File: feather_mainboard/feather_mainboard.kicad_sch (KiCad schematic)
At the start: 0 parts

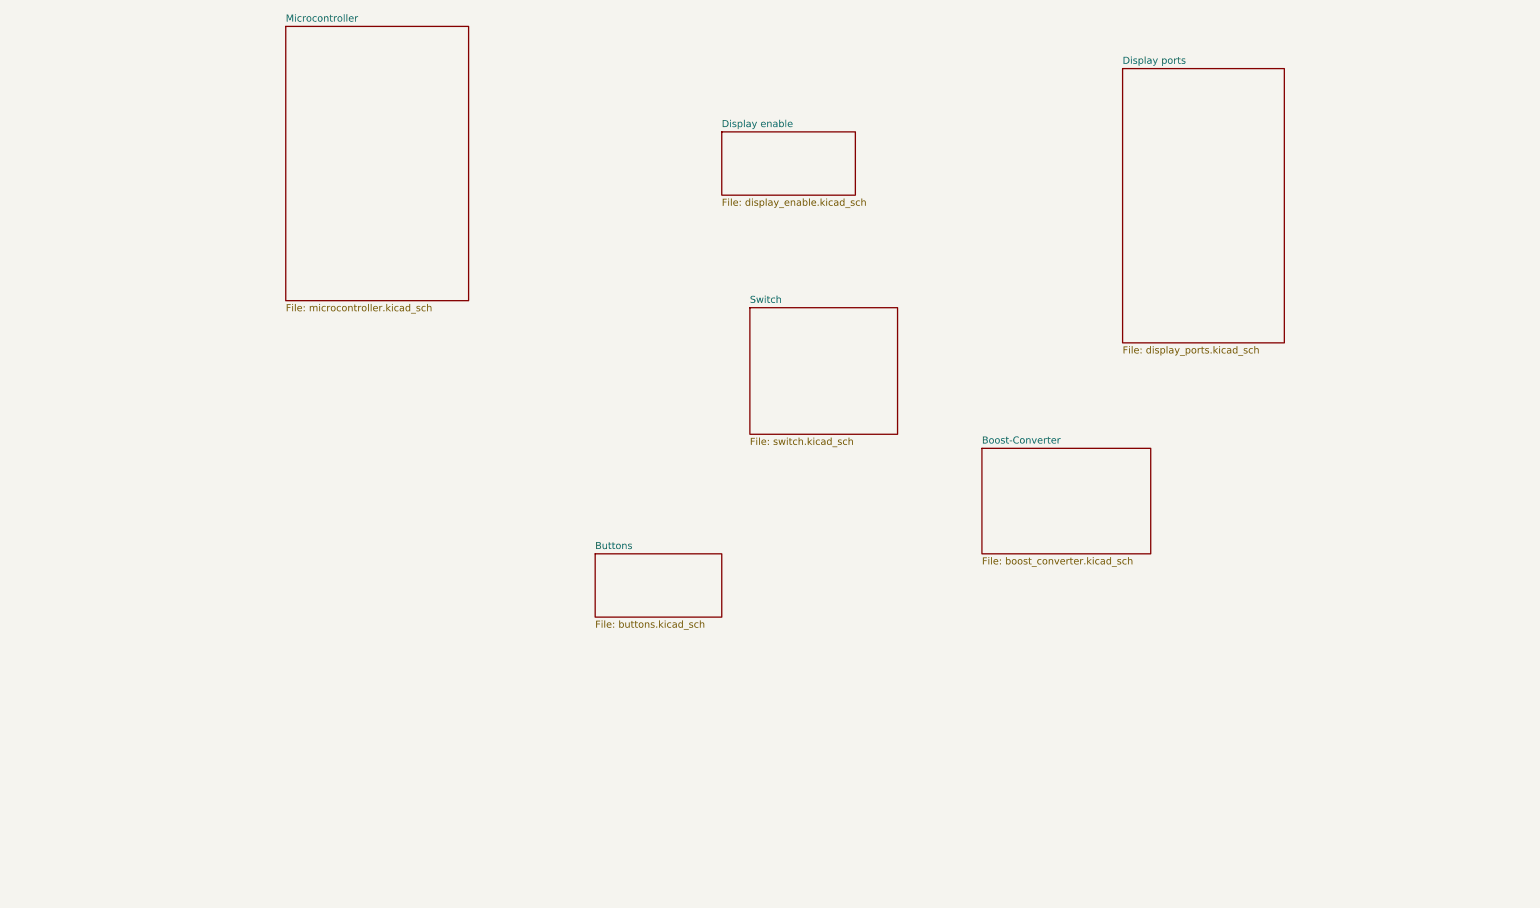
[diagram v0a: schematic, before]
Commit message: finished microcontroller and microsd card subsheets. TODO: button subsheets and internal connections
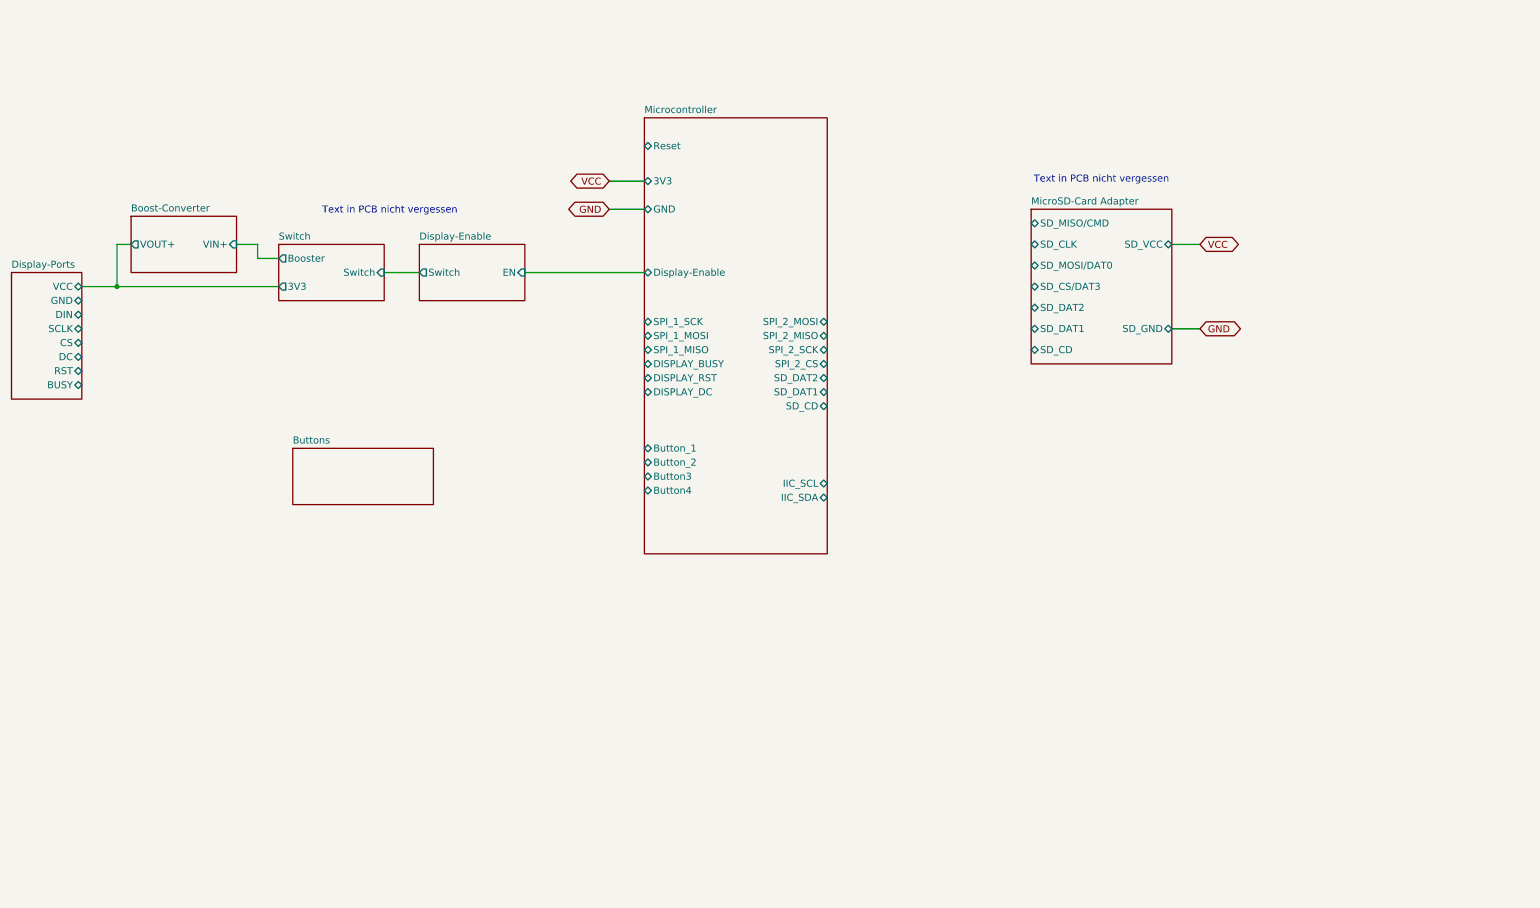
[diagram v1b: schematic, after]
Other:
- sheet Display enable renamed Display-Enable
- sheet Display ports renamed Display-Ports
- added sheet MicroSD-Card Adapter (microsd-card_adapter.kicad_sch)
- sheet Boost-Converter ports: added VIN+, VOUT+; removed none
- sheet Display-Enable ports: added EN, Switch; removed none
- sheet Display-Ports ports: added BUSY, CS, DC, DIN, GND, RST, SCLK, VCC; removed none
- sheet Microcontroller ports: added 3V3, Button3, Button4, Button_1, Button_2, DISPLAY_BUSY, DISPLAY_DC, DISPLAY_RST, Display-Enable, GND, IIC_SCL, IIC_SDA, Reset, SD_CD, SD_DAT1, SD_DAT2, SPI_1_MISO, SPI_1_MOSI, SPI_1_SCK, SPI_2_CS, SPI_2_MISO, SPI_2_MOSI, SPI_2_SCK; removed none
- sheet Switch ports: added 3V3, Booster, Switch; removed none
- note added: "Text in PCB nicht vergessen"

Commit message: schematic is almost done (check TODOs in schematic file)
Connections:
- no-connect marks 0 -> 3
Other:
- added sheet Reset-Button (reset-button.kicad_sch)
- sheet Buttons ports: added Button_1, Button_2, Button_3; removed none
- sheet Microcontroller ports: added Button_3, DISPLAY_CS, DISPLAY_MOSI, DISPLAY_SCLK, Free, SD_CLK, SD_CS/DAT3, SD_MISO/CMD, SD_MOSI/DAT0; removed Button3, Button4, SPI_1_MISO, SPI_1_MOSI, SPI_1_SCK, SPI_2_CS, SPI_2_MISO, SPI_2_MOSI, SPI_2_SCK
- note added: "TODOs: Schematic: - Change the buttons to the correct ones!!! - Pogo-Pin Magnets PCB Design: - Mounting Holes - Messpunkte - Text in PCB für Switches schreiben"
- note removed: "Text in PCB nicht vergessen"

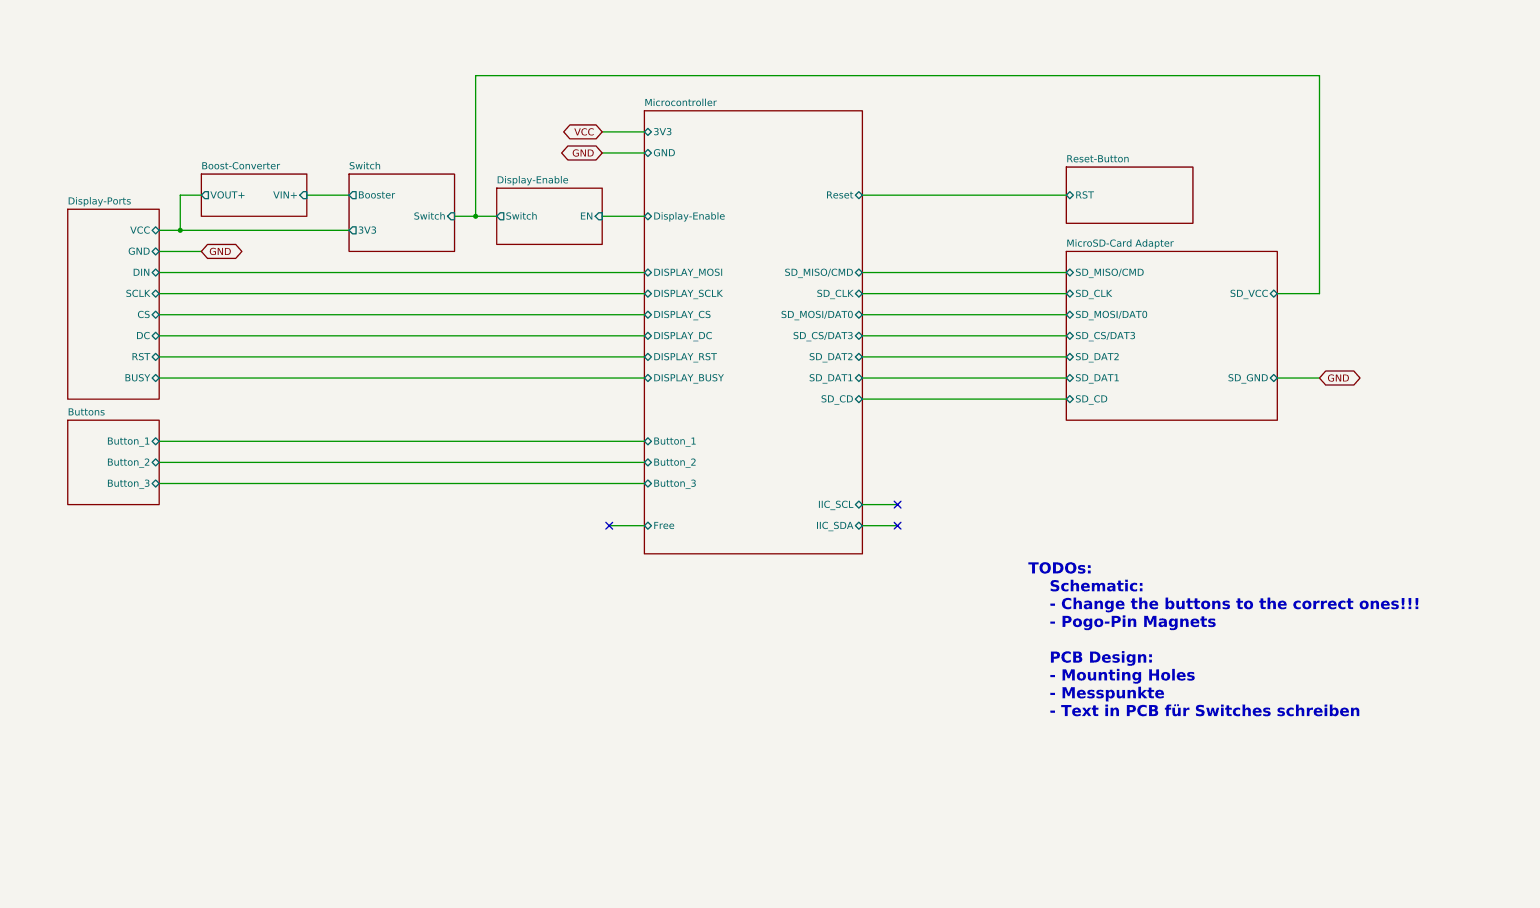
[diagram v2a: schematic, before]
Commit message: added daughter board
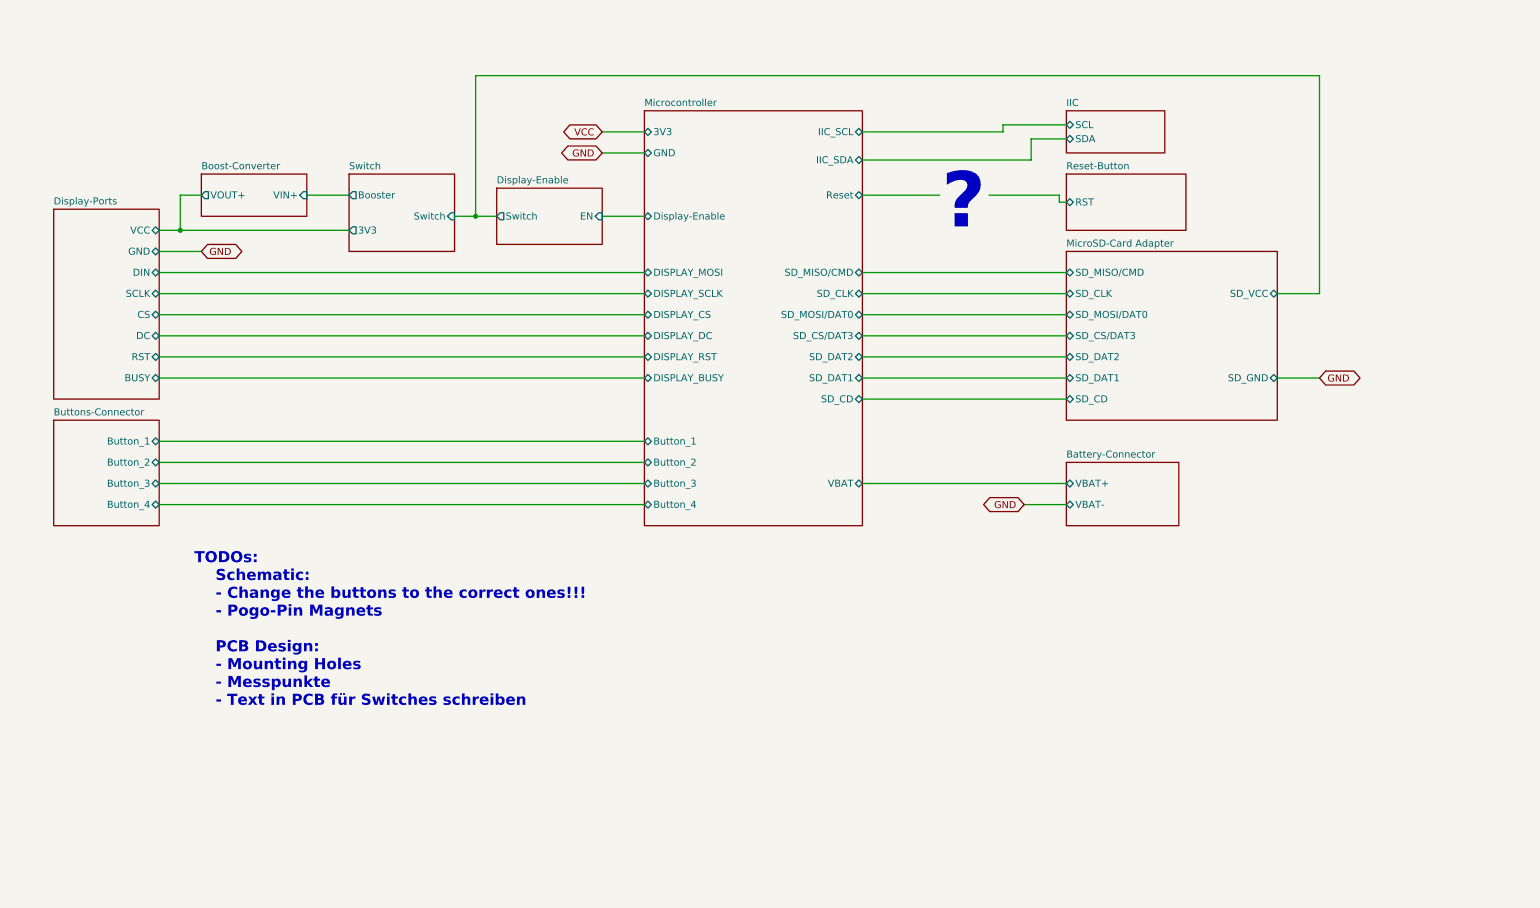
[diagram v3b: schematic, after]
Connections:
- no-connect marks 3 -> 0
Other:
- sheet Buttons renamed Buttons-Connector
- added sheet Battery-Connector (battery-connector.kicad_sch)
- added sheet IIC (iic.kicad_sch)
- sheet Buttons-Connector: file buttons.kicad_sch -> buttons-connector.kicad_sch
- sheet Buttons-Connector ports: added Button_4; removed none
- sheet Microcontroller ports: added Button_4, VBAT; removed Free
- note added: "?"

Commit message: finished daughter board
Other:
- note added: "Nummerierung!"
- note removed: "TODOs: Schematic: - Change the buttons to the correct ones!!! - Pogo-Pin Magnets PCB Design: - Mounting Holes - Messpunkte - Text in PCB für Switches schreiben"
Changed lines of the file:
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@@
+	(wire
+		(pts
+			(xy 172.72 59.69) (xy 177.8 59.69)
+		)
+		(stroke
+			(width 0)
+			(type default)
+		)
+	)
 	(wire
 		(pts
@@
 	(wire
 		(pts
+			(xy 179.07 60.96) (xy 179.07 63.5)
+		)
+		(stroke
+			(width 0)
+			(type default)
+		)
+	)
+	(wire
+		(pts
 			(xy 45.72 88.9) (xy 133.35 88.9)
 		)
@@
 	(wire
 		(pts
-			(xy 198.12 59.69) (xy 198.12 58.42)
-		)
-		(stroke
-			(width 0)
-			(type default)
-		)
-	)
-	(wire
-		(pts
 			(xy 172.72 71.12) (xy 186.69 71.12)
 		)
@@
 	(wire
 		(pts
-			(xy 172.72 59.69) (xy 198.12 59.69)
+			(xy 177.8 58.42) (xy 209.55 58.42)
 		)
 		(stroke
@@
 	(wire
 		(pts
+			(xy 179.07 63.5) (xy 172.72 63.5)
+		)
+		(stroke
+			(width 0)
+			(type default)
+		)
+	)
+	(wire
+		(pts
 			(xy 172.72 104.14) (xy 209.55 104.14)
 		)
@@
 	(wire
 		(pts
-			(xy 203.2 64.77) (xy 203.2 60.96)
-		)
-		(stroke
-			(width 0)
-			(type default)
-		)
-	)
-	(wire
-		(pts
-			(xy 198.12 58.42) (xy 209.55 58.42)
+			(xy 177.8 59.69) (xy 177.8 58.42)
 		)
 		(stroke
@@
 	(wire
 		(pts
-			(xy 172.72 64.77) (xy 203.2 64.77)
-		)
-		(stroke
-			(width 0)
-			(type default)
-		)
-	)
-	(wire
-		(pts
-			(xy 203.2 60.96) (xy 209.55 60.96)
+			(xy 179.07 60.96) (xy 209.55 60.96)
 		)
 		(stroke
@@
 		)
 	)
-	(text "TODOs:\n	Schematic:\n	- Change the buttons to the correct ones!!!\n	- Pogo-Pin Magnets\n\n	PCB Design:\n	- Mounting Holes\n	- Messpunkte\n	- Text in PCB für Switches schreiben"
+	(text "Nummerierung!"
 		(exclude_from_sim no)
-		(at 52.07 149.606 0)
+		(at 153.416 146.558 0)
 		(effects
 			(font
-				(size 2 2)
-				(thickness 0.4)
+				(size 10 10)
 				(bold yes)
 			)
-			(justify left)
 		)
 	)
@@
 		)
 		(pin "IIC_SDA" bidirectional
-			(at 172.72 64.77 0)
-			(effects
-				(font
+			(at 172.72 63.5 0)
+			(effects
+				(font

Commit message: finished mainboard design, need to do the routing
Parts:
- added H1, H2, H3, H4: MountingHole_Pad, MountingHole:MountingHole_2.2mm_M2_DIN965_Pad, symbol Mechanical:MountingHole_Pad
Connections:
- net GND: now also H1.1, H2.1, H3.1, H4.1
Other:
- removed sheet Battery-Connector
- sheet Microcontroller ports: added none; removed VBAT
- note added: "C1_x -> 100 nF C2_x -> 10 µF C3_x -> 470 pF C4_x -> 4.7 µF"
- note added: "R1_x -> 10 kΩ R2_x -> 180 Ω R3_x -> 75 kΩ"
- note removed: "?"
- note removed: "Nummerierung!"
